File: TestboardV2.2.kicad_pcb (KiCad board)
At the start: 2 copper layers, 61 x 100 mm, 147 parts, among them IC1 BME680, IC2 MAX17048G+, IC3 LTC2954CTS8-1#TRMPBF, IC4 CN3791, IC5 FS312F-G, J1 Conn_01x04, J10 Conn_01x02, J11 Conn_01x02, J13 USB_C_Receptacle_USB2.0 USB41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, J2 Conn_01x04_MountingPin, J3 Conn_01x04_MountingPin, J4 Conn_01x04_MountingPin, J5 Conn_01x04_MountingPin, J6 Conn_01x04_MountingPin, J7 Conn_01x04, J8 Conn_01x02, J9 Conn_01x03, Q1 UMH3N, Q2 DMG2301L, Q3 AO3401A, Q4 FS8205, Q5 AO3400, SW1 SW_Push, SW2 SW_Push, SW3 SW_Push, U1 ESP32-WROOM-32D, U10 PC817, U11 PC817, U12 CP2102N-A02-GQFN24, U13 XC6220B331MR, U14 MCP73831-2-OT, U2 PC817, U3 PC817, U4 PC817, U5 PC817, U6 PC817, U7 PC817, U8 PC817, U9 PC817

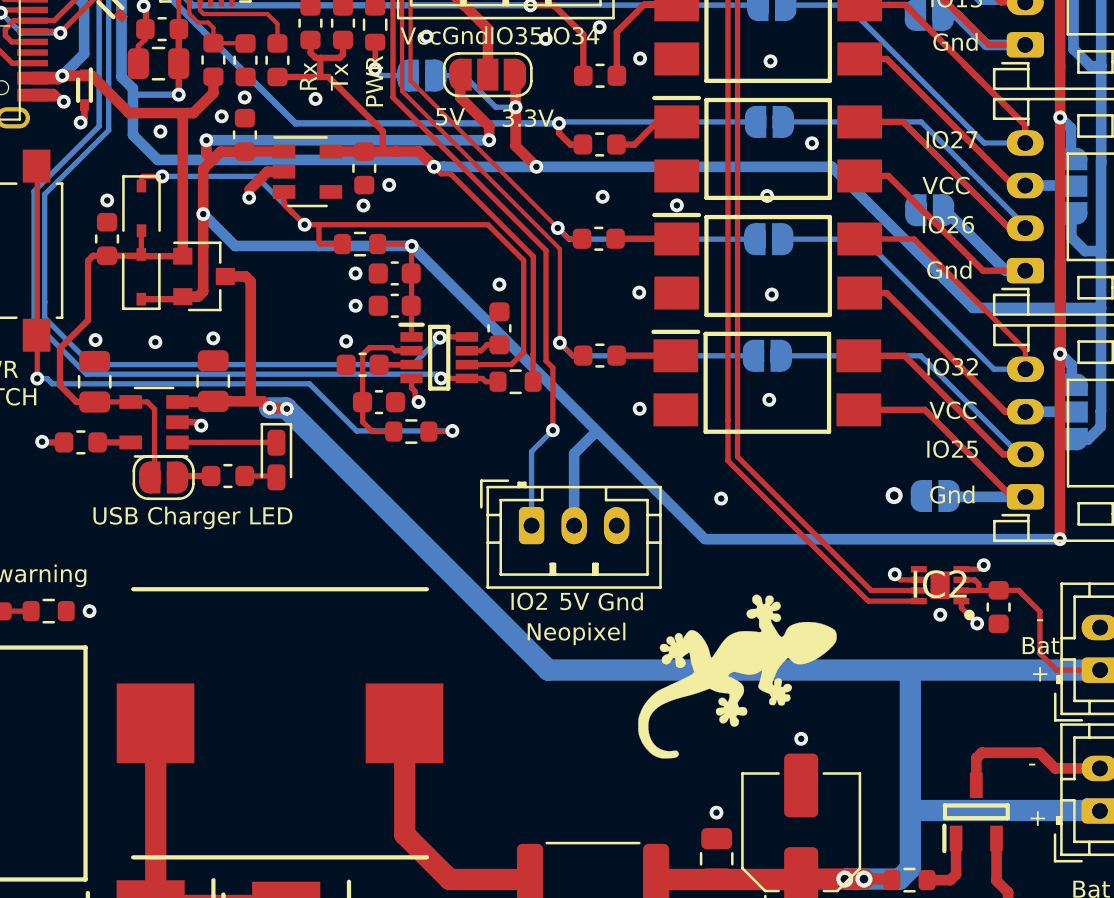
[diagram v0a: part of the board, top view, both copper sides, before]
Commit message: Added LDO CE Pullup. JLCPCB files updated
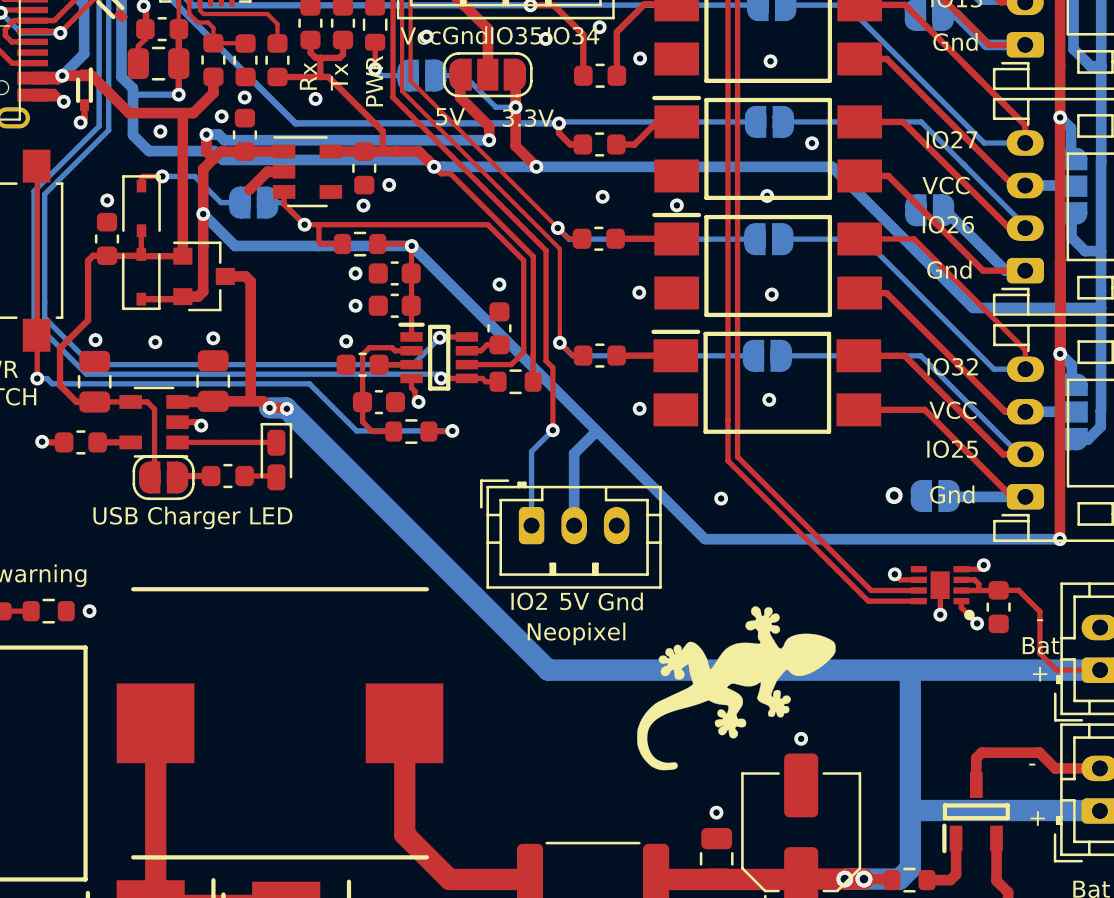
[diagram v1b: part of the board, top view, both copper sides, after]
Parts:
- removed the REF** at (105.5, 135.3)
- added JP24: SolderJumper_2_Open, Jumper:SolderJumper-2_P1.3mm_Open_RoundedPad1.0x1.5mm, B.Cu at (114.7, 120.2)
- added REF**: WEEE-Logo_4.2x6mm_SilkScreen, Symbol:WEEE-Logo_4.2x6mm_SilkScreen, B.Cu at (102.0, 93.4)
- added REF**: OSHW-Logo2_7.3x6mm_SilkScreen, Symbol:OSHW-Logo2_7.3x6mm_SilkScreen, B.Cu at (108.0, 93.9)
- D15: value LED -> LED Green
- R23: renamed from R30; value TBD -> 140K
- R27: renamed from R28; value TBD -> 10K
- R29: value 1K -> 10K
- moved G*** 5.55 mm to (131.1, 150.8), turned to 180 degrees
- moved G*** 0.55 mm to (137.3, 143.1)
- renumbered C13 to C12, C14 to C13, C19 to C14, C12 to C18, C18 to C19, C20 to C21, C21 to C22, C22 to C23, C23 to C25, C24 to C26, C25 to C27, D12 to D10, D13 to D11, D14 to D12, D9 to D13, D4 to D14, D5 to D4, D8 to D5, D10 to D8, D11 to D9, J1 to J10, J10 to J12, R17 to R16, R18 to R17, R19 to R18, R20 to R19, R23 to R20, R25 to R24, R27 to R25, R31 to R28, R32 to R30, R35 to R31, R36 to R32, R24 to R35, R16 to R36, SW3 to SW4, U14 to U15
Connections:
- D14 pad 1: CE -> Net-(D14-Pad1)
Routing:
- net CE: track 31.5 -> 24.7 mm, vias 2 -> 1
- net Net-(D14-Pad1): track 0.00 -> 5.94 mm, vias 0 -> 1
- net GND: track 29.2 -> 30.6 mm, vias 205 -> 204
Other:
- board text added: "- Solar in +"
- board text added: "Auto PWR by USB-C"
- board text removed: "+ Solar in -"
